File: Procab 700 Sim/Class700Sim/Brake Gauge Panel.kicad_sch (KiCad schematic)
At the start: 12 parts, among them SW27 SW-DMIL, SW28 SW-DMIR, SW29 SW-EMG, SW30 SW-DRA, SW31 SW-PCB, SW32 SW-MDAC, SW33 SW-MDDC, SW34 SW-PSON, SW35 SW-PSOF

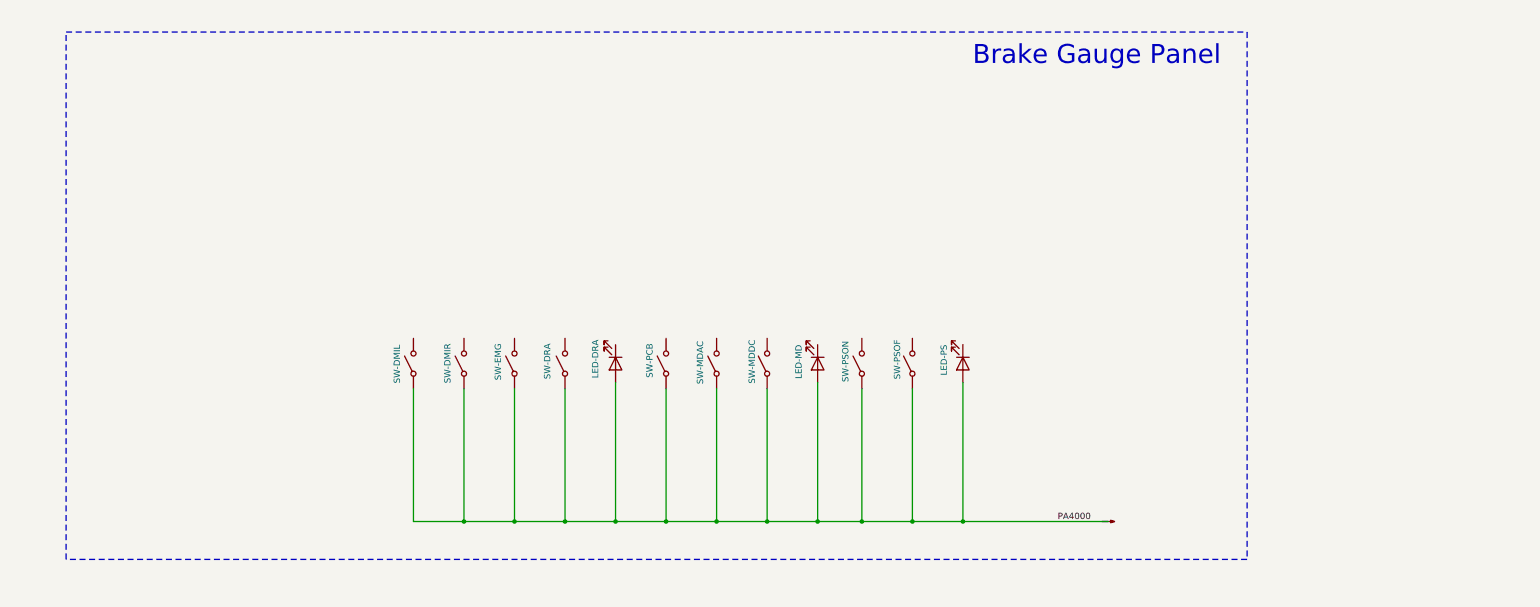
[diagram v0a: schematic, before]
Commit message: Drew the air gauge panel
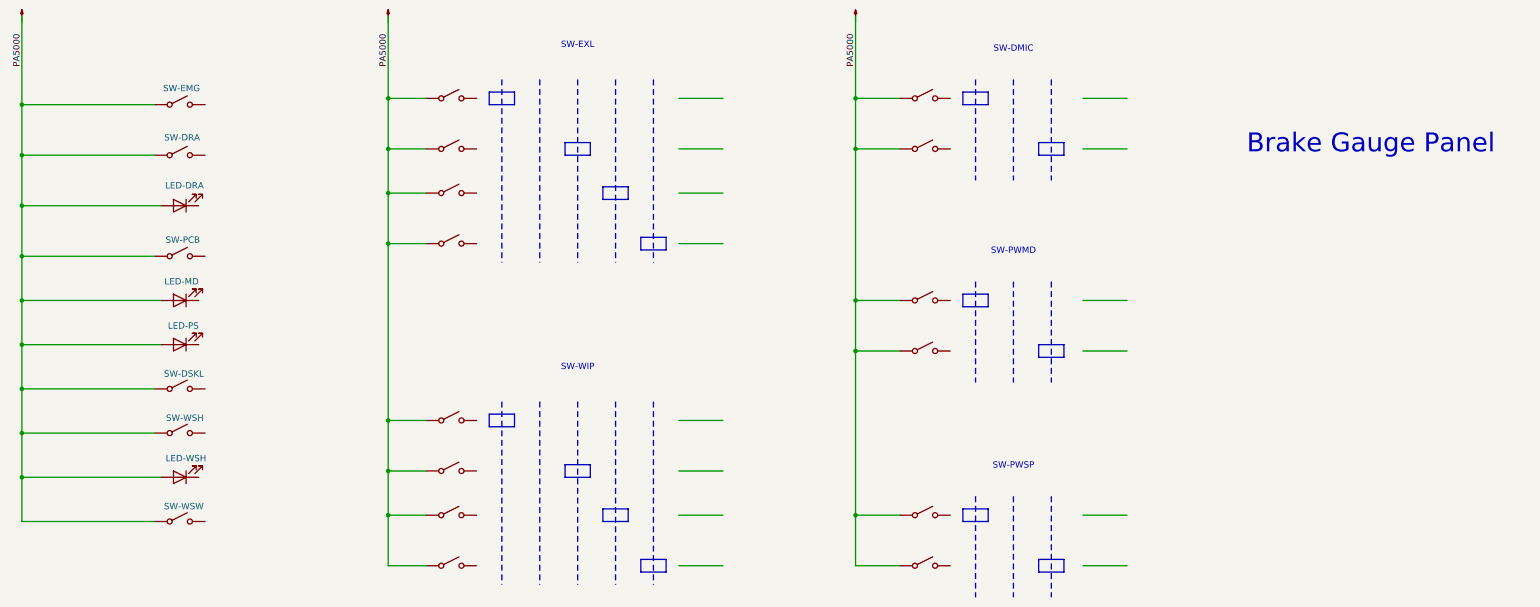
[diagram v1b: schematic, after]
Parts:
- removed SW27: SW-DMIL, symbol Switch:SW_SPST
- removed SW28: SW-DMIR, symbol Switch:SW_SPST
- removed SW32: SW-MDAC, symbol Switch:SW_SPST
- removed SW33: SW-MDDC, symbol Switch:SW_SPST
- removed SW34: SW-PSON, symbol Switch:SW_SPST
- removed SW35: SW-PSOF, symbol Switch:SW_SPST
- added D8: LED-WSH, symbol Device:LED
- added SW36: SW-DSKL, symbol Switch:SW_SPST
- added SW37: SW-WSH, symbol Switch:SW_SPST
- added SW38: SW-WSW, symbol Switch:SW_SPST
- added SW39, SW40, SW41, SW42, SW43, SW44, SW45, SW46, SW47, SW48, SW49, SW50, SW51, SW52: SWAWS, symbol Switch:SW_SPST
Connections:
- net PA4000 is gone; now on net PA5000: D5.2 (A), D6.2 (A), D7.2 (A), SW29. (B), SW30. (B), SW31. (B)
- net PA5000: now reaches SW31. (B)
- net PA5000: now also D8.2 (A), SW36. (B), SW37. (B), SW38. (B), SW39. (B), SW40. (B), SW41. (B), SW42. (B), SW43. (B), SW44. (B), SW45. (B), SW46. (B), SW47. (B), SW48. (B), SW49. (B), SW50. (B), SW51. (B), SW52. (B)
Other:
- note added: "SW-DMIC"
- note added: "SW-EXL"
- note added: "SW-PWMD"
- note added: "SW-PWSP"
- note added: "SW-WIP"

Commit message: Changes made
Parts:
- added D10: LED-HZRD, symbol Device:LED
- added D11: LED-MJAL, symbol Device:LED
- added D4: LED-HVEM, symbol Device:LED
- added D9: LED-FIRE, symbol Device:LED
- added SW22: SW-CBHD, symbol Switch:SW_SPST
- added SW23: SW-FIRE, symbol Switch:SW_SPST
- added SW24: SW-HZRD, symbol Switch:SW_SPST
- added SW25: SW-MJAL, symbol Switch:SW_SPST
- added SW7, SW8: SWAWS, symbol Switch:SW_SPST
- added SW9: SW-HVEM, symbol Switch:SW_SPST
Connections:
- net DX1D-04: now reaches D6.1 (K)
- net DX1D-06: now reaches D8.1 (K)
- net DX1D-03: now reaches D5.1 (K)
- net DX1D-05: now reaches D7.1 (K)
- new net DX1B-03: SW29. (B)
- new net DX1B-04: SW30. (B)
- new net DX1B-05: SW31. (B)
- new net DX1B-10: SW36. (B)
- new net DX1B-15: SW37. (B)
- new net DX1B-16: SW38. (B)
- new net DX1C-07: SW22. (B)
- new net DX1C-08: SW9. (B)
- new net DX1C-09: SW23. (B)
- new net DX1C-10: SW24. (B)
- new net DX1C-11: SW25. (B)
- new net DX1D-07: D4.1 (K)
- new net DX1D-08: D9.1 (K)
- new net DX1D-09: D10.1 (K)
- new net DX1D-10: D11.1 (K)
- new net PA6000: D10.2 (A), D11.2 (A), D4.2 (A), D9.2 (A), SW22. (B), SW23. (B), SW24. (B), SW25. (B), SW7. (B), SW8. (B), SW9. (B)
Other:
- note added: "SW-CBL"
